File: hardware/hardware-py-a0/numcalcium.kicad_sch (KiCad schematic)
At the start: 2 parts

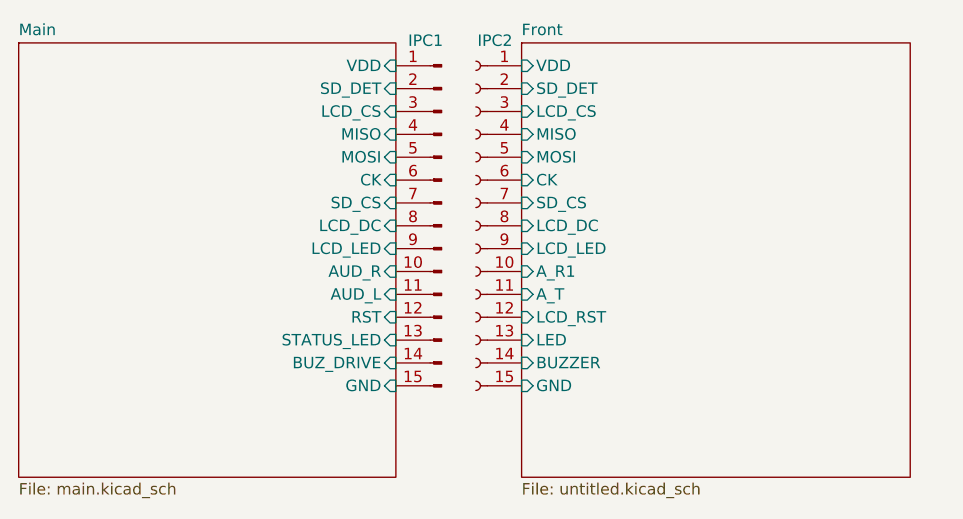
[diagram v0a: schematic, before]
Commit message: hardware: py/a0 revision 1.1 using FFC connectors
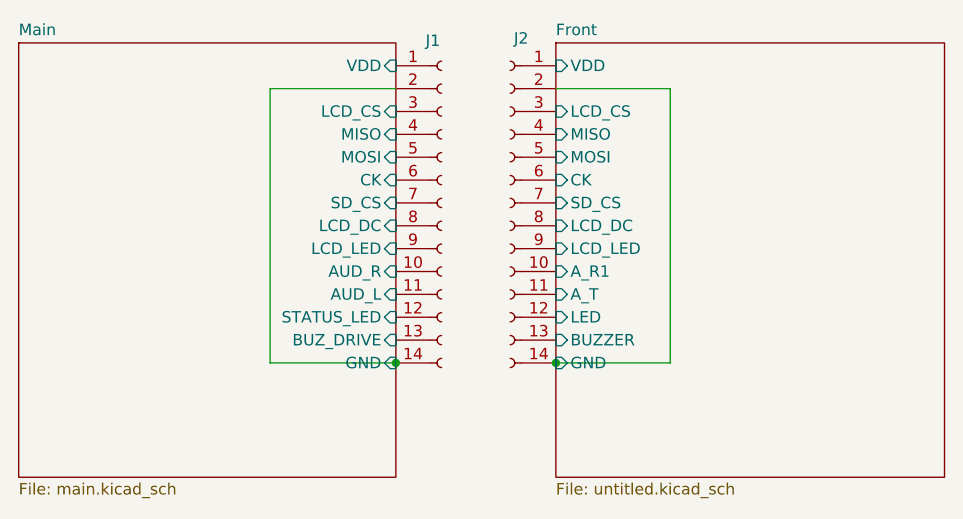
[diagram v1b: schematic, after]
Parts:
- removed IPC1: Conn_01x16_Pin, Connector_PinHeader_2.54mm:PinHeader_1x15_P2.54mm_Vertical, symbol Connector:Conn_01x15_Pin
- removed IPC2: Conn_01x16_Socket, footprints:PinSocket_1x15_P2.54mm_Vertical_Pads, symbol Connector:Conn_01x15_Socket
- added J1, J2: Conn_01x14_Socket, Connector_FFC-FPC:Hirose_FH12-14S-0.5SH_1x14-1MP_P0.50mm_Horizontal, symbol Connector:Conn_01x14_Socket
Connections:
- net Front/A_R1: now also J2.10 (Pin_10)
- net Front/A_T: now also J2.11 (Pin_11)
- net Front/BUZZER: now also J2.13 (Pin_13)
- net Front/CK: now also J2.6 (Pin_6)
- net Front/GND: now also J2.14 (Pin_14), J2.2 (Pin_2)
- net Front/LCD_CS: now also J2.3 (Pin_3)
- net Front/LCD_DC: now also J2.8 (Pin_8)
- net Front/LCD_LED: now also J2.9 (Pin_9)
- net Front/LED: now also J2.12 (Pin_12)
- net Front/MISO: now also J2.4 (Pin_4)
- net Front/MOSI: now also J2.5 (Pin_5)
- net Front/SD_CS: now also J2.7 (Pin_7)
- net Front/VDD: now also J2.1 (Pin_1)
- net Main/AUD_L: now also J1.11 (Pin_11)
- net Main/AUD_R: now also J1.10 (Pin_10)
- net Main/BUZ_DRIVE: now also J1.13 (Pin_13)
- net Main/CK: now also J1.6 (Pin_6)
- net Main/GND: now also J1.14 (Pin_14), J1.2 (Pin_2)
- net Main/LCD_CS: now also J1.3 (Pin_3)
- net Main/LCD_DC: now also J1.8 (Pin_8)
- net Main/LCD_LED: now also J1.9 (Pin_9)
- net Main/MISO: now also J1.4 (Pin_4)
- net Main/MOSI: now also J1.5 (Pin_5)
- net Main/SD_CS: now also J1.7 (Pin_7)
- net Main/STATUS_LED: now also J1.12 (Pin_12)
- net Main/VDD: now also J1.1 (Pin_1)
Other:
- sheet Front ports: added none; removed LCD_RST, SD_DET
- sheet Main ports: added none; removed RST, SD_DET
- company: (none) -> MOTIV.PW
